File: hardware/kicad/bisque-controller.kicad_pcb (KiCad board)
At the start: 2 copper layers, 125 x 100 mm, 141 parts, among them J1 USB-C, J10 AUX, J11 INPUTS, J12 CT, J13 AC_SENSE_DNP, J14 QWIIC, J2 5V_IN, J3 TC1_K, J4 SSR1, J5 DISPLAY, J6 NAV_SW, J7 AUX, J8 TC2_K, J9 SSR2, Q2 AO3400A, Q3 AO3400A, SW1 RESET, SW2 BOOT, U1 ESP32-S3-WROOM-1U-N16R2, U2 AMS1117-3.3, U3 MAX31856MUD+, U4 USBLC6-2SC6, U5 MAX31856MUD+, U6 ULN2003A, U7 ADE7953ACPZ, U8 LTV-817S-TA1-C, U9 LTV-817S-TA1-C, Y1 3.579545MHz

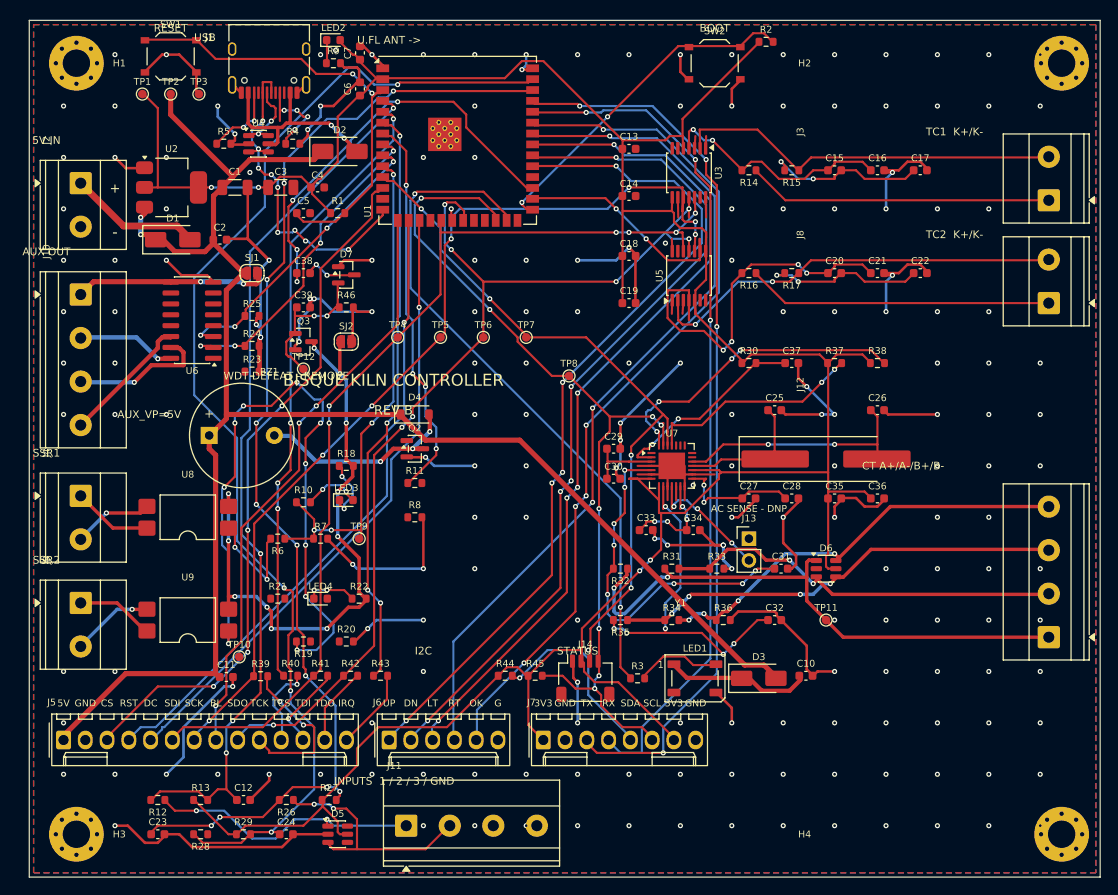
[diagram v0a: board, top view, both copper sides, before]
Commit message: feat(hw): rev B goes 4-layer — 0 DRC errors, 0 unconnected
Rung 3 of spec 6.3's escalation ladder. 2-layer did not close at any rung;
this is the measured result of the stack-up change the user approved.

Stack-up: F.Cu and B.Cu carry signals only, In1.Cu is an unbroken GND plane,
In2.Cu is the +3V3 plane. Both signal-layer GND pours are gone — on rev B's
density they were the largest single consumer of routing space on exactly the
two layers the boxed-in signals needed. Every SMD pad of a plane net now drops
a via straight to its plane instead (109 of them); through-hole pads reach it
by existing.

In2 carries +3V3 alone rather than being split with +5V. A split needs the two
nets' consumers to fall in separable regions and +5V's do not — regulator at
the top-left corner, LCD header at the bottom edge, buzzer mid-board, LED
supply at the right — so a partition following them would leave +3V3, the net
that actually needs the plane, in slivers. +5V routes comfortably as 0.6 mm
track.

The isolation barrier keepout is now AllCuMask(4), inner planes included: a
GND plane under the optocouplers would defeat the barrier completely.
check_pcb.py grew an independent confirmation that samples the band against
each plane's filled polygons, because a zone fill is not a track and none of
the item-based checks could see one.

Four generator bugs fixed, all latent and all found by this work:

- The final "exact hop to the true terminal" segment was emitted after the A*
  search and was the only copper on the board no clearance check ever saw. It
  is what put EN 0.195 mm from U1 pad 4 on the rung-2 board. The goal is now
  any of the nine nodes around the terminal whose hop is clearance-legal.
- miter_corners() chamfered corners that had a via on them, silently orphaning
  the via and stranding everything beyond it (two dangling vias and a 7.4 mm
  SSR_EN track on the first 4-layer build).
- The USB D- seed never touched J1.B7: the link crossed 1.5 mm south of the
  pad it was s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
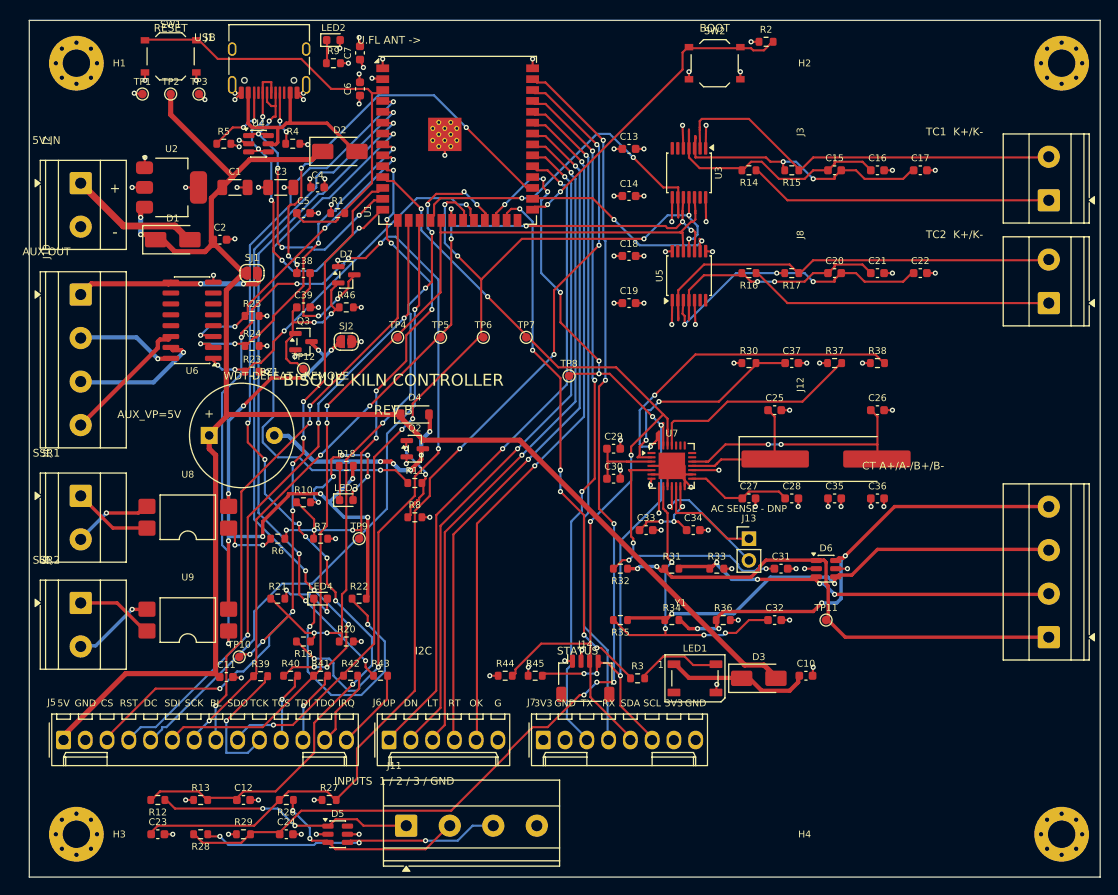
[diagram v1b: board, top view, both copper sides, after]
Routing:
- net +3V3: track 361.9 -> 45.7 mm, vias 4 -> 35
- net GND: track 387.6 -> 93.3 mm, vias 193 -> 74
- net SSR2_CTRL: track 0.00 -> 84.2 mm, vias 0 -> 10
- net SSR2_LED_A: track 77.2 -> 132.1 mm, vias 10 -> 8
- net AUX1: track 0.00 -> 42.0 mm, vias 0 -> 4
- net TC1_CS: track 2.34 -> 42.3 mm, vias 0 -> 2
- net IN3_RAW: track 0.00 -> 36.5 mm, vias 0 -> 3
- net USB_DN: track 9.15 -> 39.2 mm, vias 2 -> 5
- net TXD0: track 105.3 -> 80.5 mm, vias 4 -> 3
- net SSR2_IND_K: track 5.99 -> 30.2 mm
- net RXD0: track 99.5 -> 78.0 mm, vias 3 -> 1
- net BTN_DOWN: track 99.5 -> 78.6 mm, vias 5 -> 2
- net BTN_UP: track 98.9 -> 78.1 mm, vias 5 -> 2
- net BTN_LEFT: track 100.0 -> 79.3 mm, vias 5 -> 2
- net BTN_RIGHT: track 100.5 -> 79.9 mm, vias 3 -> 2
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- added copper zone on In2.Cu, net +3V3
- added copper zone on In1.Cu, net GND
- removed copper zone on B.Cu, net GND
- removed copper zone on F.Cu, net GND
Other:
- copper layers 2 -> 4

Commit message: feat(hw): walk rev B back to 100 x 100 mm — still 0 DRC errors
Rung 2 of spec 6.3's ladder recovered. With GND and +3V3 on inner planes the
board no longer needs the extra 25 mm the 2-layer attempt bought: at
100 x 100 mm it routes with 0 unrouted nets on the FIRST pass, where 125 x 100
needed a promotion pass. That returns the bare board to JLCPCB's <= 100 x 100
promo tier (~$2-4 for 5 pcs against ~$10-15).

The 25 mm came out of the analog column, so that column is re-floorplanned:

- East-edge screw terminals J3/J8/J12 move from x 139 to x 114, and the
  mounting-hole grid returns to 90 x 90 (H2/H4 at x 114.5).
- ANA1E/ANA2E go from a 31 mm single row to a 7 mm two-column block; ANA3T,
  ANA3U, ANA3E and BOT1 all end at x 107.6, clear of the terminals.
- Y1 leaves the east side, where a 20.3 mm HC49-SD land pattern no longer
  fits, and goes to the bottom of ANA3S. It is deliberately BELOW the CT
  front-end rows rather than immediately south of U7: at y 77.5 it walled off
  the whole south escape corridor of the QFN, which is where CTB_F, ADE_VN,
  ADE_VP and ADE_REF leave.
- U7's four decoupling caps become a single column in the 5.6 mm ANA3E strip.

check_placement: 0 courtyard overlaps, 0 parts off-board. KiCad DRC: 0
unconnected pads, 0 errors, 0 footprint errors. The 92 violations are all
silkscreen (68 overlap, 22 over-copper, 2 edge) - more than the 125 mm board's
62, which is what packing the same parts into 80% of the area does to
reference designators. Not a fab blocker; rev A shipped with the same class.
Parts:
- moved H2 26.0 mm to (114.5, 25.0)
- moved H4 26.0 mm to (114.5, 115.0)
- moved Y1 25.7 mm to (96.8, 91.2)
- moved J12 25.0 mm to (114.0, 92.0)
- moved J3 25.0 mm to (114.0, 41.0)
- moved J8 25.0 mm to (114.0, 53.0)
- moved C22 21.7 mm to (103.0, 55.0)
- moved C17 21.5 mm to (103.0, 42.0)
- moved C36 14.2 mm to (104.8, 76.2)
- moved C21 13.0 mm to (106.1, 51.0)
- moved C16 12.9 mm to (106.1, 38.0)
- moved C26 12.9 mm to (106.1, 65.5)
- moved R38 12.9 mm to (106.1, 60.0)
- moved C20 11.4 mm to (102.7, 51.0)
- moved C15 11.4 mm to (102.7, 38.0)
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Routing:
- net ADE_VINTA: track 12.4 -> 58.8 mm, vias 0 -> 4
- net ADE_CLKIN: track 16.0 -> 55.5 mm, vias 0 -> 4
- net CTB_N: track 54.8 -> 26.7 mm, vias 4 -> 2
- net CTA_P: track 59.0 -> 31.5 mm, vias 2 -> 0
- net I2C_SCL: track 101.7 -> 128.5 mm, vias 11 -> 9
- net CTB_P: track 54.4 -> 28.1 mm
- net TC1_N: track 47.3 -> 21.3 mm
- net TC2_N: track 51.5 -> 27.8 mm
- net CTA_N: track 45.9 -> 22.5 mm, vias 4 -> 1
- net TC2_P: track 35.6 -> 12.8 mm
- net TC1_P: track 35.6 -> 13.4 mm
- net ADE_REF: track 11.6 -> 31.8 mm, vias 3 -> 2
- net ADE_CS: track 40.7 -> 22.1 mm
- net TC1_P_F: track 30.1 -> 15.5 mm, vias 0 -> 2
- net TC2_P_F: track 29.9 -> 16.1 mm
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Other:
- board size 125 x 100 mm -> 100 x 100 mm

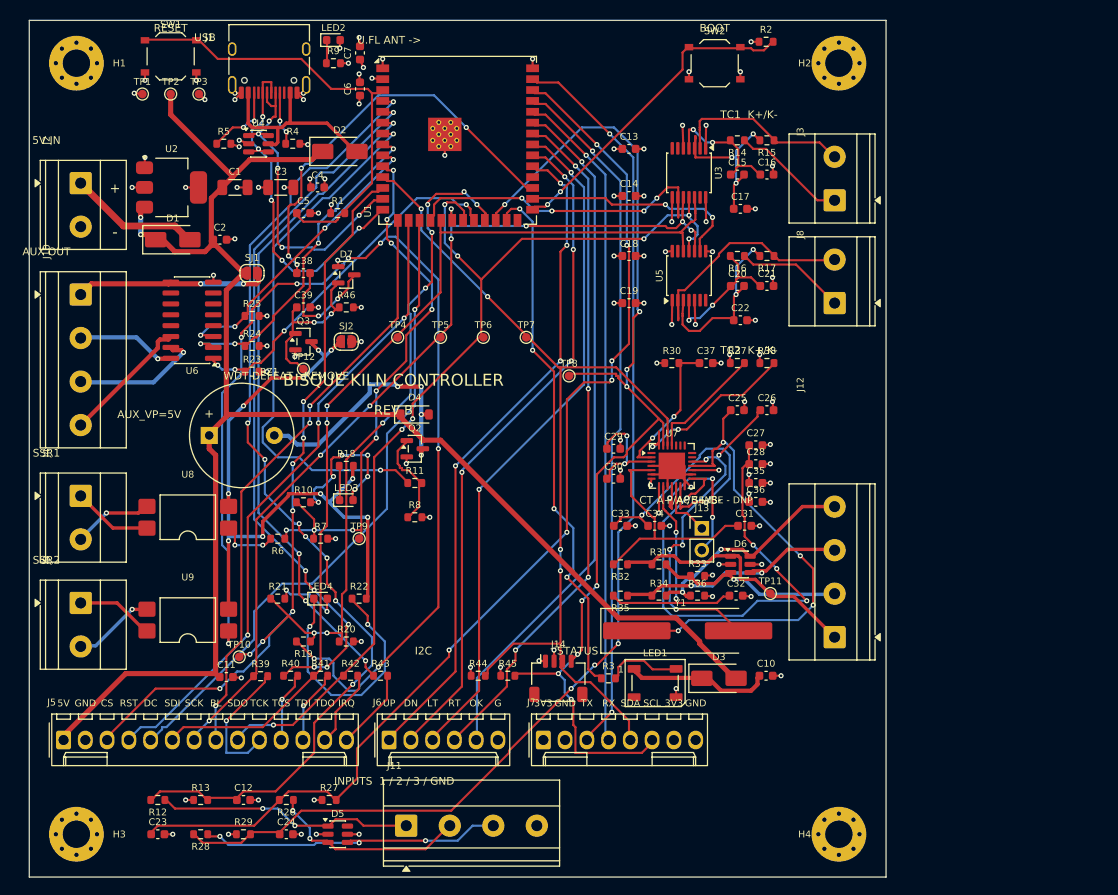
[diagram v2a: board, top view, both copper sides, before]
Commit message: feat(hw): walk rev B back to 0805 passives — still 0 DRC errors
Rung 1 of spec 6.3's ladder recovered, so rev B is back on rev A's passive
size: easier hand-rework, and gen_jlc.py keeps rev A's 0805 LCSC part numbers
for R1-R13/C1-C12 instead of having to re-pick every line in 0603.

Two placement consequences of the bigger courtyards, both found by
check_placement/the router rather than guessed:

- U7's decoupling no longer fits as a column of four in the 5.6 mm ANA3E
  strip (4 x 2.55 mm > 8.7 mm), so C36 moves up into ANA3U.
- U4's row had R5 and R4 hard against it, and at 0805 that closed the 0.4 mm
  VBUS lane into U4 completely - the one net that would not route. Splitting
  the row (R5 and R4 drop to y 33.4, D2 to 36.5) reopens it.

0 courtyard overlaps, 0 parts off-board, 0 unrouted nets, 0 unconnected pads,
0 DRC errors, 0 footprint errors. 102 silkscreen warnings, up from 92 at 0603
- larger parts, same silk.
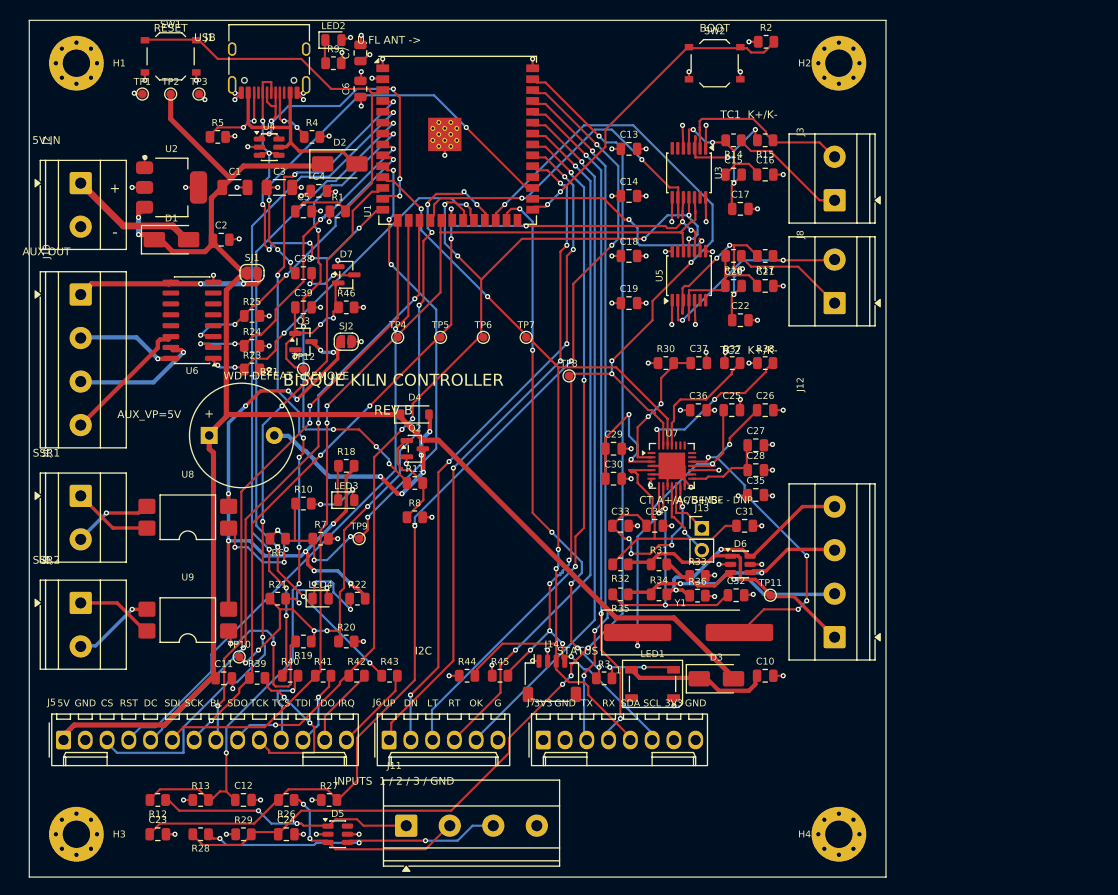
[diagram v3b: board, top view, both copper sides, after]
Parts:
- C10, C11, C12, C13, C14, C15, C16, C17, C18, C19, C2, C20, C21, C22, C23, C24, C25, C26, C27, C28, C29, C30, C31, C32, C33, C34, C35, C36, C37, C38, C39, C4, C5, C6, C7: footprint C_0603_1608Metric -> C_0805_2012Metric
- LED2, LED3, LED4: footprint LED_0603_1608Metric -> LED_0805_2012Metric
- R1, R10, R11, R12, R13, R14, R15, R16, R17, R18, R19, R2, R20, R21, R22, R23, R24, R25, R26, R27, R28, R29, R3, R30, R31, R32, R33, R34, R35, R36, R37, R38, R39, R4, R40, R41, R42, R43, R44, R45, R46, R5, R6, R7, R8, R9: footprint R_0603_1608Metric -> R_0805_2012Metric
- moved C36 12.6 mm to (98.1, 65.5)
- moved R4 2.39 mm to (53.0, 33.6)
- moved D2 1.45 mm to (56.2, 36.8)
- moved C35 1.40 mm to (104.8, 75.4)
- moved U4 1.31 mm to (48.0, 34.8)
- moved R44 1.30 mm to (71.1, 96.5)
- moved R5 1.06 mm to (42.0, 33.6)
- moved R43 1.05 mm to (62.0, 96.5)
- moved R45 0.90 mm to (75.0, 96.5)
- moved C37 0.85 mm to (98.2, 60.0)
- moved J14 0.75 mm to (81.0, 96.8)
- moved C28 0.70 mm to (104.8, 72.5)
- moved R30 0.70 mm to (94.3, 60.0)
- moved R42 0.70 mm to (58.2, 96.5)
- moved C25 0.65 mm to (102.0, 65.5)
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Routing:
- net SSR2_LED_A: track 132.1 -> 20.5 mm, vias 8 -> 2
- net ADE_VINTA: track 58.8 -> 9.91 mm, vias 4 -> 0
- net SSR2_IND_K: track 30.2 -> 9.35 mm
- net ADE_CLKIN: track 55.5 -> 37.2 mm, vias 4 -> 2
- net SSR1_IND_A: track 18.0 -> 6.79 mm, vias 6 -> 2
- net IN1: track 117.1 -> 106.8 mm
- net ADE_VN: track 18.7 -> 8.97 mm, vias 3 -> 1
- net ADE_REF: track 31.8 -> 22.8 mm, vias 2 -> 4
- net SSR1_LED_A: track 6.82 -> 14.7 mm, vias 2 -> 4
- net T_CS: track 84.7 -> 77.6 mm, vias 6 -> 4
- net WDT_PUMP: track 13.7 -> 6.96 mm
- net ALARM: track 62.9 -> 56.3 mm, vias 2 -> 6
- net TC2_N_F: track 21.4 -> 27.5 mm, vias 2 -> 4
- net GND: track 93.2 -> 98.6 mm
- net I2C_SCL: track 128.5 -> 133.0 mm, vias 9 -> 10
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
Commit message: feat(hw): rev B back on rev A's net classes — 0.3 mm signal, 0.7 mm power
The last of the three concessions the 2-layer attempt made. Signals go from
0.25 mm back to 0.3 mm and +5V/VLED/AUX_VP from 0.5-0.6 mm to 0.7 mm; VIN was
already 0.8. +3V3 and GND are better off than rev A ever was — they are whole
copper layers now, not 0.7 mm tracks.

The geometric constraint that forced 0.25 mm has not gone away: a 0.5 mm-pitch
QFN-28 or 0.65 mm-pitch TSSOP-14 pad can only be left along its own
centreline. What changed is that the router never touches those pads. Each is
represented to it by the far end of its fanout stub, so 0.25 mm is confined to
the ~2 mm of escape that requires it (FANOUT_WIDTH, PLANE_STUB_W) and the rest
of every net runs at full width.

Widening the power rails exposed a second unchecked code path in the router,
the same class of bug as the terminal hop: A* took a via on via_ok() alone,
which answers for the 0.6 mm barrel and not for the track that resumes on the
far layer, so the first segment after a via was never clearance-checked at its
start point. At 0.25 mm the error hid inside the via's own envelope; at 0.7 mm
it put AUX_VP 0.172 mm from SJ1 pad 1 (KiCad DRC caught it, my checker did
not — check_pcb models a custom-shaped solder-jumper pad by its (size) field,
which understates it). The via branch now requires blocked() on the
destination layer too.

100 x 100 mm, 0805, 0.3/0.7 mm: 0 unrouted nets, 0 unconnected pads, 0 DRC
errors, 0 footprint errors, 102 silkscreen warnings. Two consecutive builds
are byte-identical, board and DRC report alike.

All three rungs of spec 6.3's ladder are now given back: the 4-layer stack-up
paid for every one of them.
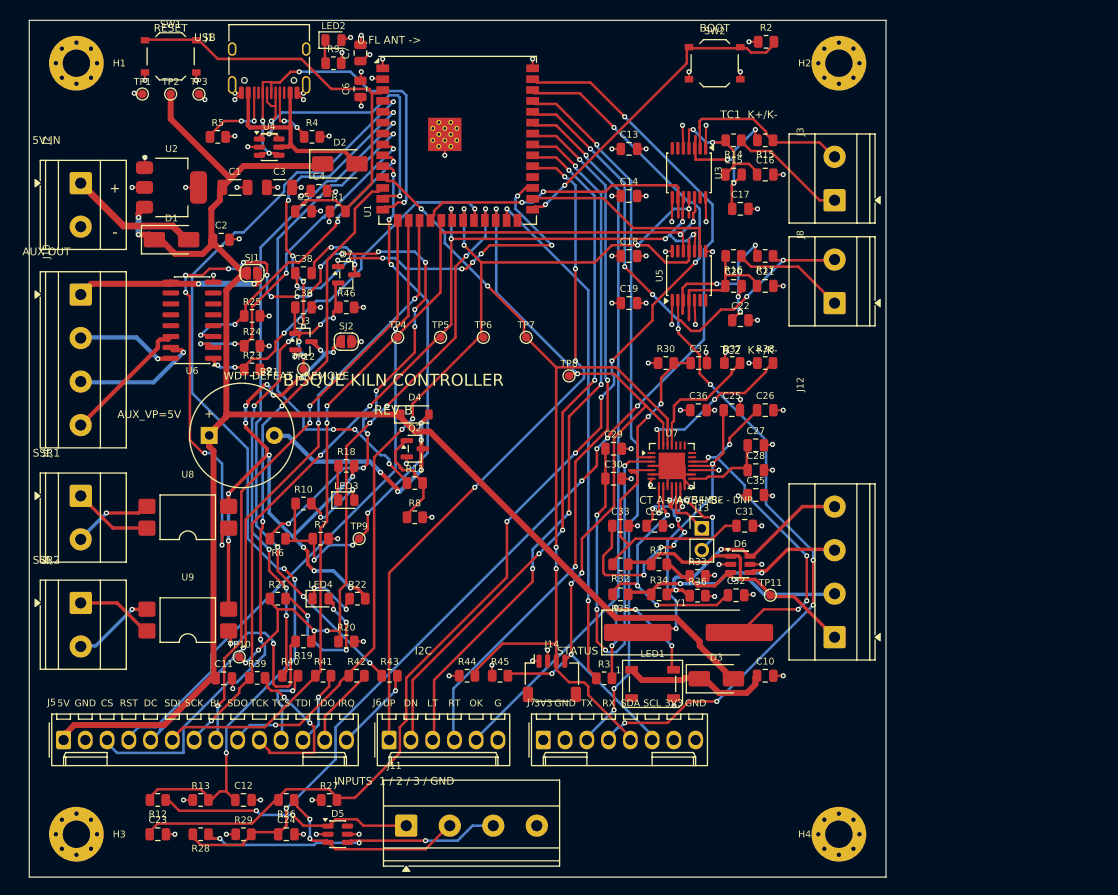
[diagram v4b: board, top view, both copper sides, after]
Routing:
- net SSR1_LED_A: track 14.7 -> 114.8 mm, vias 4 -> 20
- net I2C_SCL: track 133.0 -> 96.6 mm, vias 10 -> 6
- net ADE_VINTD: track 17.6 -> 51.4 mm, vias 2 -> 4
- net RXD0: track 78.9 -> 103.2 mm, vias 3 -> 9
- net IN2: track 126.4 -> 138.2 mm, vias 4 -> 6
- net WS_DIN: track 8.96 -> 19.7 mm, vias 2 -> 4
- net SSR2_IND_A: track 8.23 -> 17.7 mm, vias 2 -> 4
- net IN1: track 106.8 -> 115.0 mm, vias 8 -> 4
- net ADE_REF: track 22.8 -> 30.8 mm, vias 4 -> 7
- net WDT_KICK: track 51.1 -> 44.3 mm, vias 4 -> 8
- net SSR2_CTRL: track 85.1 -> 79.1 mm, vias 10 -> 8
- net TC1_CS: track 42.7 -> 36.9 mm
- net ADE_VN: track 8.97 -> 13.8 mm, vias 1 -> 3
- net USB_DP: track 42.9 -> 46.3 mm, vias 7 -> 4
- net TXD0: track 80.2 -> 83.5 mm
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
